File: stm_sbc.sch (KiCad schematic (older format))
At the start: 2 parts, among them U1 ATmega328-PU, U2 ATmega328-PU

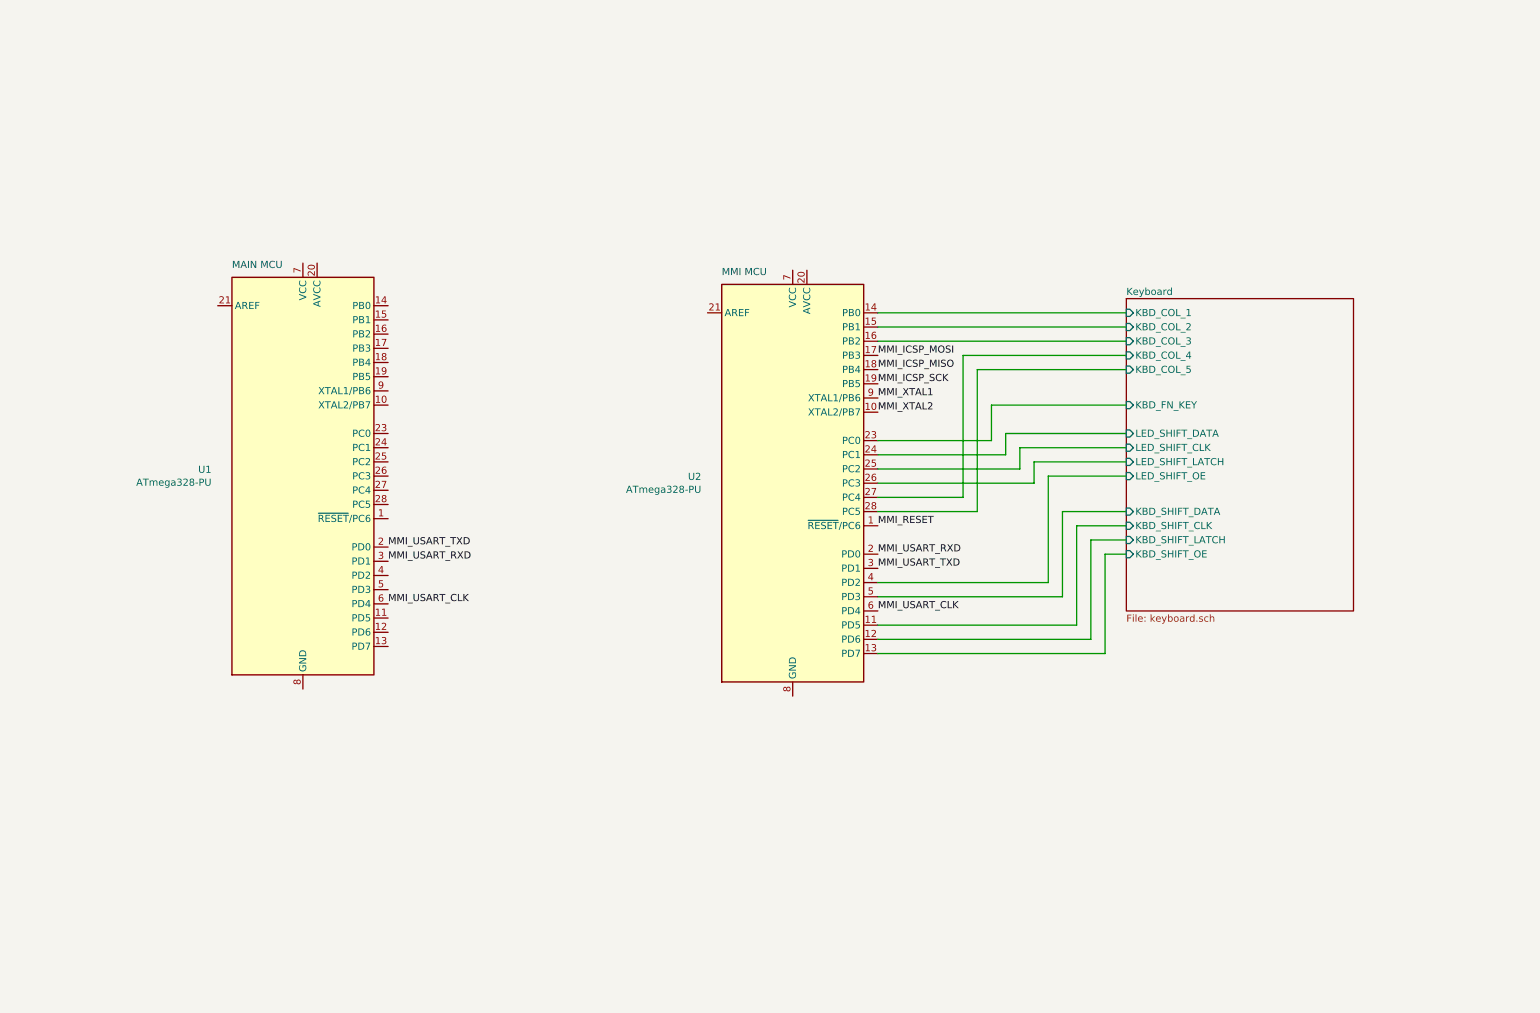
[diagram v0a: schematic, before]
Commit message: atmega128 and external memory
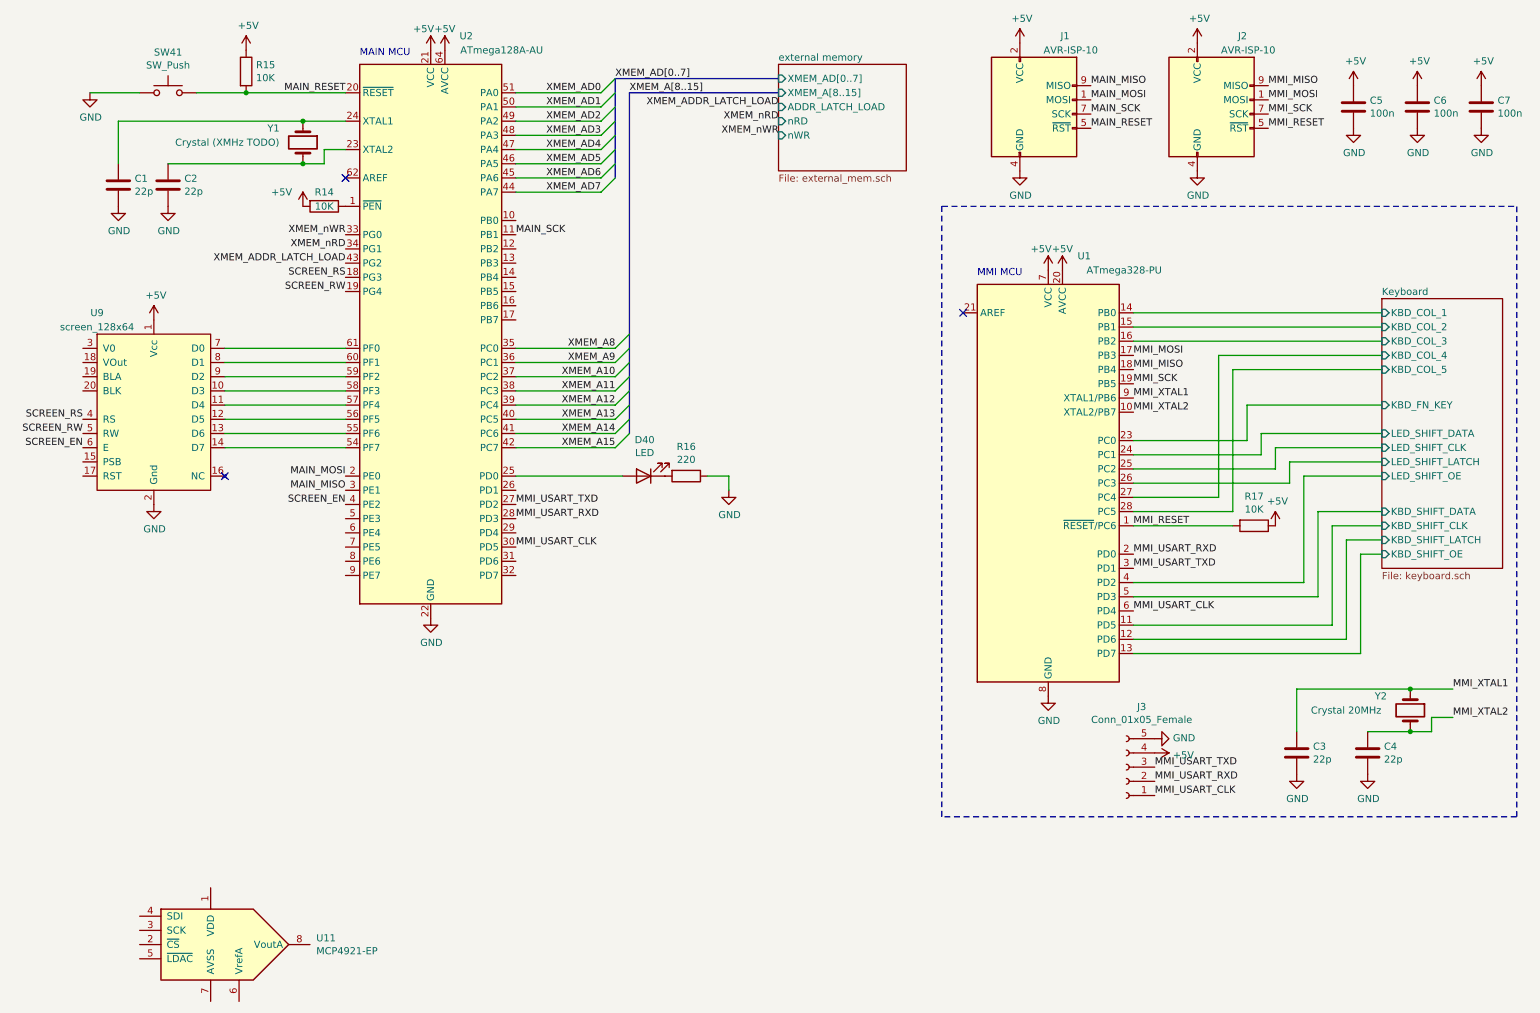
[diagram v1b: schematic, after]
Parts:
- removed U1: ATmega328-PU, Package_DIP:DIP-28_W7.62mm, symbol MCU_Microchip_ATmega:ATmega328-PU
- added C1, C2, C3, C4: 22p, Capacitor_THT:C_Disc_D3.0mm_W1.6mm_P2.50mm, symbol Device:C
- added C5, C6, C7: 100n, symbol Device:C
- added D40: LED, LED_THT:LED_D5.0mm, symbol Device:LED
- added J1, J2: AVR-ISP-10, Connector_PinHeader_2.54mm:PinHeader_2x05_P2.54mm_Vertical, symbol Connector:AVR-ISP-10
- added J3: Conn_01x05_Female, symbol Connector:Conn_01x05_Female
- added R14, R15, R17: 10K, Resistor_THT:R_Axial_DIN0207_L6.3mm_D2.5mm_P7.62mm_Horizontal, symbol Device:R
- added R16: 220, Resistor_THT:R_Axial_DIN0207_L6.3mm_D2.5mm_P7.62mm_Horizontal, symbol Device:R
- added SW41: SW_Push, symbol Switch:SW_Push
- added U11: MCP4921-EP, symbol Analog_DAC:MCP4921-EP
- added U2: ATmega128A-AU, Package_QFP:TQFP-64_14x14mm_P0.8mm, symbol MCU_Microchip_ATmega:ATmega128A-AU
- added U9: screen_128x64, Connector_PinHeader_2.54mm:PinHeader_1x20_P2.54mm_Vertical, symbol stm_sbc_symbols:screen_128x64
- added Y1: Crystal (XMHz TODO), symbol Device:Crystal
- added Y2: Crystal 20MHz, symbol Device:Crystal
- renumbered U2 to U1
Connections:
- net MMI_RESET: now also J2.5 (~RST), R17.2
- net MMI_USART_CLK: now also J3.1 (Pin_1), U2.30 (PD5)
- net MMI_USART_RXD: now also J3.2 (Pin_2), U2.28 (PD3)
- net MMI_USART_TXD: now also J3.3 (Pin_3), U2.27 (PD2)
- net MMI_XTAL1: now also C3.2, Y2.1
- net MMI_XTAL2: now also C4.2, Y2.2
- net +5V: now reaches U1.20 (AVCC)
- net +5V: now also U1.7 (VCC), C5.1, C6.1, C7.1, J1.2 (VCC), J2.2 (VCC), J3.4 (Pin_4), R14.2, R15.1, R17.1, U2.21 (VCC), U2.52 (VCC), U2.64 (AVCC), U9.1 (Vcc)
- net GND: now reaches U1.22 (GND), U1.8 (GND)
- net GND: now also C1.1, C2.1, C3.1, C4.1, C5.2, C6.2, C7.2, J1.10 (GND), J1.4 (GND), J1.6 (GND), J1.8 (GND), J2.10 (GND), J2.4 (GND), J2.6 (GND), J2.8 (GND), J3.5 (Pin_5), R16.1, SW41.1, U2.22 (GND), U2.53 (GND), U2.63 (GND), U9.2 (Gnd)
- net MMI_ICSP_MISO renamed MMI_MISO
- net MMI_MISO: now also J2.9 (MISO)
- net MMI_ICSP_MOSI renamed MMI_MOSI
- net MMI_MOSI: now also J2.1 (MOSI)
- net MMI_ICSP_SCK renamed MMI_SCK
- net MMI_SCK: now also J2.7 (SCK)
- new net: R14.1, U2.1 (~PEN)
- new net: C2.2, U2.23 (XTAL2), Y1.2
- new net: C1.2, U2.24 (XTAL1), Y1.1
- new net: D40.2 (A), U2.25 (PD0)
- new net: U2.54 (PF7), U9.14 (D7)
- new net: U2.55 (PF6), U9.13 (D6)
- new net: U2.56 (PF5), U9.12 (D5)
- new net: U2.57 (PF4), U9.11 (D4)
- new net: U2.58 (PF3), U9.10 (D3)
- new net: U2.59 (PF2), U9.9 (D2)
- new net: U2.60 (PF1), U9.8 (D1)
- new net: U2.61 (PF0), U9.7 (D0)
- new net: D40.1 (K), R16.2
- new net MAIN_MISO: J1.9 (MISO), U2.3 (PE1)
- new net MAIN_MOSI: J1.1 (MOSI), U2.2 (PE0)
- new net MAIN_RESET: J1.5 (~RST), R15.2, SW41.2, U2.20 (~RESET)
- new net MAIN_SCK: J1.7 (SCK), U2.11 (PB1)
- new net SCREEN_EN: U2.4 (PE2), U9.6 (E)
- new net SCREEN_RS: U2.18 (PG3), U9.4 (RS)
- new net SCREEN_RW: U2.19 (PG4), U9.5 (RW)
- new net XMEM_A10: U2.37 (PC2)
- new net XMEM_A11: U2.38 (PC3)
- new net XMEM_A12: U2.39 (PC4)
- new net XMEM_A13: U2.40 (PC5)
- new net XMEM_A14: U2.41 (PC6)
- new net XMEM_A15: U2.42 (PC7)
- new net XMEM_A8: U2.35 (PC0)
- new net XMEM_A9: U2.36 (PC1)
- new net XMEM_AD0: U2.51 (PA0)
- new net XMEM_AD1: U2.50 (PA1)
- new net XMEM_AD2: U2.49 (PA2)
- new net XMEM_AD3: U2.48 (PA3)
- new net XMEM_AD4: U2.47 (PA4)
- new net XMEM_AD5: U2.46 (PA5)
- new net XMEM_AD6: U2.45 (PA6)
- new net XMEM_AD7: U2.44 (PA7)
- new net XMEM_ADDR_LATCH_LOAD: U2.43 (PG2)
- new net XMEM_nRD: U2.34 (PG1)
- new net XMEM_nWR: U2.33 (PG0)
- no-connect marks 0 -> 3
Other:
- moved on the sheet: U1
